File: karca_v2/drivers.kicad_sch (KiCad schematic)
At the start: 15 parts, among them J10 Keyhole ignition switch, J8 Screw_Terminal_01x10, J9 Screw_Terminal_01x04, Q7 IRF3708

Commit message: updated
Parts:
- removed D24: D_Schottky, Diode_SMD:D_SMA, symbol Device:D_Schottky

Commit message: Version alpha
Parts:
- removed BZ1: Buzzer, symbol Device:Buzzer
- removed Q7: IRF3708, symbol Simulation_SPICE:NMOS
- added F7: Fuse, Fuse:Fuse_1812_4532Metric, symbol Device:Fuse
- added J12: Buzzer, terminal blocks:P-2604-1102, symbol Connector:Screw_Terminal_01x02
- added Q4: IRF3708, IRF3708:TO254P1041X444X1930-3, symbol Simulation_SPICE:NMOS
- J10: footprint (none) -> terminal blocks:P-2604-1102
- J11: renamed from J9; footprint (none) -> terminal blocks:P-2604-1104
- J9: renamed from J8; footprint (none) -> terminal blocks:P-2604-1110
- R12: renamed from R3; value 910 -> 1k; footprint (none) -> Resistor_SMD:R_1206_3216Metric
- R13: renamed from R34; value 910 -> 1k; footprint (none) -> Resistor_SMD:R_1206_3216Metric
- R14: renamed from R44; footprint (none) -> Resistor_SMD:R_1206_3216Metric
- R15: renamed from R45; footprint (none) -> Resistor_SMD:R_1206_3216Metric
- R16: renamed from R39; footprint (none) -> Resistor_SMD:R_1206_3216Metric
- R17: renamed from R40; footprint (none) -> Resistor_SMD:R_1206_3216Metric
- TP22: renamed from TP42; footprint (none) -> TestPoint:TestPoint_Pad_D2.0mm
- renumbered D5 to D7, D23 to D8
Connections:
- net +12V: now also F7.1; no longer D7.2 (A), D8.2 (A), J10.1 (Pin_1)
- net GND: now also J12.2 (Pin_2), Q4.3 (S)
- net IGN_POS: now reaches J10.2 (Pin_2), J11.2 (Pin_2)
- net IGN_POS: now also D7.2 (A), D8.2 (A), J10.1 (Pin_1), F7.2, J12.1 (Pin_1)
- net IGN_NEG: now reaches J11.3 (Pin_3), R14.1
- net IGN_NEG: now also R13.2, Q4.2 (D)
- net at R16.2, TP22.1: now also Q4.1 (G)
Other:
- sheet current monitor ports: added DRV1_ADC, DRV2_ADC, DRV3_ADC, DRV4_ADC, DRV5_ADC, DRV5_TVS; removed CS, DRV_CLK, DRV_MISO, DRV_MOSI
- moved on the sheet: D7, D8, R12, R13, R14, R15, R16, R17, TP22

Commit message: discrete traces
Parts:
- renumbered F7 to F2, Q4 to Q3
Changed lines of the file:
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@@
   (symbol (lib_id "power:+12V") (at 214.63 135.89 0) (unit 1)
     (in_bom yes) (on_board yes) (dnp no) (fields_autoplaced)
-    (property "Reference" "#PWR052" (at 214.63 139.7 0)
+    (property "Reference" "#PWR063" (at 214.63 139.7 0)
       (effects (font (size 1.27 1.27)) hide)
     )
@@
       (project "karca_v2"
         (path "/29cf4797-56f2-4f57-ae95-7df639362e3c/7dac9c60-d103-4efb-8cad-8e42b4335148"
-          (reference "#PWR052") (unit 1)
+          (reference "#PWR063") (unit 1)
         )
       )
@@
   (symbol (lib_id "power:GND") (at 78.74 180.34 0) (unit 1)
     (in_bom yes) (on_board yes) (dnp no) (fields_autoplaced)
-    (property "Reference" "#PWR057" (at 78.74 186.69 0)
+    (property "Reference" "#PWR068" (at 78.74 186.69 0)
       (effects (font (size 1.27 1.27)) hide)
     )
@@
       (project "karca_v2"
         (path "/29cf4797-56f2-4f57-ae95-7df639362e3c/7dac9c60-d103-4efb-8cad-8e42b4335148"
-          (reference "#PWR057") (unit 1)
+          (reference "#PWR068") (unit 1)
         )
       )
@@
   (symbol (lib_id "power:GND") (at 140.335 174.625 0) (unit 1)
     (in_bom yes) (on_board yes) (dnp no) (fields_autoplaced)
-    (property "Reference" "#PWR056" (at 140.335 180.975 0)
+    (property "Reference" "#PWR067" (at 140.335 180.975 0)
       (effects (font (size 1.27 1.27)) hide)
     )
@@
       (project "karca_v2"
         (path "/29cf4797-56f2-4f57-ae95-7df639362e3c/7dac9c60-d103-4efb-8cad-8e42b4335148"
-          (reference "#PWR056") (unit 1)
+          (reference "#PWR067") (unit 1)
         )
       )
@@
   (symbol (lib_id "power:GND") (at 68.58 153.67 0) (unit 1)
     (in_bom yes) (on_board yes) (dnp no) (fields_autoplaced)
-    (property "Reference" "#PWR053" (at 68.58 160.02 0)
+    (property "Reference" "#PWR065" (at 68.58 160.02 0)
       (effects (font (size 1.27 1.27)) hide)
     )
@@
       (project "karca_v2"
         (path "/29cf4797-56f2-4f57-ae95-7df639362e3c/7dac9c60-d103-4efb-8cad-8e42b4335148"
-          (reference "#PWR053") (unit 1)
+          (reference "#PWR065") (unit 1)
         )
       )
@@
   (symbol (lib_id "power:+12V") (at 78.74 128.27 0) (unit 1)
     (in_bom yes) (on_board yes) (dnp no)
-    (property "Reference" "#PWR051" (at 78.74 132.08 0)
+    (property "Reference" "#PWR062" (at 78.74 132.08 0)
       (effects (font (size 1.27 1.27)) hide)
     )
@@
       (project "karca_v2"
         (path "/29cf4797-56f2-4f57-ae95-7df639362e3c/7dac9c60-d103-4efb-8cad-8e42b4335148"
-          (reference "#PWR051") (unit 1)
+          (reference "#PWR062") (unit 1)
         )
       )
@@
   (symbol (lib_id "power:GND") (at 118.11 161.29 0) (unit 1)
     (in_bom yes) (on_board yes) (dnp no) (fields_autoplaced)
-    (property "Reference" "#PWR055" (at 118.11 167.64 0)
+    (property "Reference" "#PWR066" (at 118.11 167.64 0)
       (effects (font (size 1.27 1.27)) hide)
     )
@@
       (project "karca_v2"
         (path "/29cf4797-56f2-4f57-ae95-7df639362e3c/7dac9c60-d103-4efb-8cad-8e42b4335148"
-          (reference "#PWR055") (unit 1)
+          (reference "#PWR066") (unit 1)
         )
       )
@@
   (symbol (lib_id "Device:Fuse") (at 78.74 132.08 0) (unit 1)
     (in_bom yes) (on_board yes) (dnp no) (fields_autoplaced)
-    (property "Reference" "F7" (at 81.28 130.81 0)
+    (property "Reference" "F2" (at 81.28 130.81 0)
       (effects (font (size 1.27 1.27)) (justify left))
     )
@@
       (project "karca_v2"
         (path "/29cf4797-56f2-4f57-ae95-7df639362e3c/7dac9c60-d103-4efb-8cad-8e42b4335148"
-          (reference "F7") (unit 1)
+          (reference "F2") (unit 1)
         )
       )
@@
   (symbol (lib_id "power:GND") (at 214.63 149.86 0) (unit 1)
     (in_bom yes) (on_board yes) (dnp no) (fields_autoplaced)
-    (property "Reference" "#PWR054" (at 214.63 156.21 0)
+    (property "Reference" "#PWR064" (at 214.63 156.21 0)
       (effects (font (size 1.27 1.27)) hide)
     )
@@
       (project "karca_v2"
         (path "/29cf4797-56f2-4f57-ae95-7df639362e3c/7dac9c60-d103-4efb-8cad-8e42b4335148"
-          (reference "#PWR054") (unit 1)
+          (reference "#PWR064") (unit 1)
         )
       )
@@
   (symbol (lib_id "Simulation_SPICE:NMOS") (at 76.2 171.45 0) (unit 1)
     (in_bom yes) (on_board yes) (dnp no) (fields_autoplaced)
-    (property "Reference" "Q4" (at 81.915 170.18 0)
+    (property "Reference" "Q3" (at 81.915 170.18 0)
       (effects (font (size 1.27 1.27)) (justify left))
     )
@@
       (project "karca_v2"
         (path "/29cf4797-56f2-4f57-ae95-7df639362e3c/7dac9c60-d103-4efb-8cad-8e42b4335148"
-          (reference "Q4") (unit 1)
-        )
-      )
+          (reference "Q3") (unit 1)
+        )
+      )

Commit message: fixed violations
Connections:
- net IGN_POS: no longer J10.2 (Pin_2), J11.2 (Pin_2), J12.1 (Pin_1)
- new net IGN_POS_OUT: J10.2 (Pin_2), J11.2 (Pin_2), J12.1 (Pin_1)
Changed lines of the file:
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@@
   (junction (at 78.74 180.34) (diameter 0) (color 0 0 0 0)
   )
+  (junction (at 170.815 130.81) (diameter 0) (color 0 0 0 0)
+  )
   (junction (at 64.135 171.45) (diameter 0) (color 0 0 0 0)
   )
@@
   (junction (at 140.335 153.67) (diameter 0) (color 0 0 0 0)
   )
-  (junction (at 115.57 135.89) (diameter 0) (color 0 0 0 0)
+  (wire (pts (xy 170.815 130.81) (xy 170.815 151.13))
+    (stroke (width 0) (type default))
   )
   (wire (pts (xy 140.335 173.355) (xy 140.335 174.625))
@@
     (stroke (width 0) (type default))
   )
-  (wire (pts (xy 115.57 135.89) (xy 165.1 135.89))
-    (stroke (width 0) (type default))
-  )
   (wire (pts (xy 214.63 147.32) (xy 214.63 149.86))
     (stroke (width 0) (type default))
@@
     (stroke (width 0) (type default))
   )
-  (wire (pts (xy 115.57 156.21) (xy 118.11 156.21))
+  (wire (pts (xy 170.815 151.13) (xy 173.355 151.13))
     (stroke (width 0) (type default))
   )
@@
     (stroke (width 0) (type default))
   )
-  (wire (pts (xy 78.74 135.89) (xy 115.57 135.89))
+  (wire (pts (xy 78.74 135.89) (xy 165.1 135.89))
     (stroke (width 0) (type default))
   )
@@
     (stroke (width 0) (type default))
   )
+  (wire (pts (xy 170.815 130.81) (xy 173.355 130.81))
+    (stroke (width 0) (type default))
+  )
   (wire (pts (xy 232.41 60.96) (xy 231.14 60.96))
     (stroke (width 0) (type default))
@@
     (stroke (width 0) (type default))
   )
-  (wire (pts (xy 115.57 135.89) (xy 115.57 156.21))
+  (wire (pts (xy 173.355 153.67) (xy 173.355 156.21))
     (stroke (width 0) (type default))
   )
@@
     (stroke (width 0) (type default))
   )
-  (wire (pts (xy 167.64 130.81) (xy 173.355 130.81))
+  (wire (pts (xy 167.64 130.81) (xy 170.815 130.81))
     (stroke (width 0) (type default))
   )
   (wire (pts (xy 232.41 68.58) (xy 226.06 68.58))
-    (stroke (width 0) (type default))
-  )
-  (wire (pts (xy 118.11 158.75) (xy 118.11 161.29))
     (stroke (width 0) (type default))
   )
@@
     (effects (font (size 1.27 1.27)) (justify right bottom))
   )
-  (label "IGN_POS" (at 212.725 142.24 90) (fields_autoplaced)
+  (label "IGN_POS_OUT" (at 212.725 142.24 90) (fields_autoplaced)
     (effects (font (size 1.27 1.27)) (justify left bottom))
   )
@@
         (path "/29cf4797-56f2-4f57-ae95-7df639362e3c/7dac9c60-d103-4efb-8cad-8e42b4335148"
           (reference "#PWR076") (unit 1)
+        )
+      )
+    )
+  )
+  (symbol (lib_id "Connector:Screw_Terminal_01x02") (at 178.435 151.13 0) (unit 1)
+    (in_bom yes) (on_board yes) (dnp no)
+    (property "Reference" "J12" (at 180.975 151.13 0)
+      (effects (font (size 1.27 1.27)) (justify left))
+    )
+    (property "Value" "Buzzer" (at 175.895 156.21 0)
+      (effects (font (size 1.27 1.27)) (justify left))
+    )
+    (property "Footprint" "terminal blocks:P-2604-1102" (at 178.435 151.13 0)
+      (effects (font (size 1.27 1.27)) hide)
+    )
+    (property "Datasheet" "~" (at 178.435 151.13 0)
+      (effects (font (size 1.27 1.27)) hide)
+    )
+    (pin "2")
+    (pin "1")
+    (instances
+      (project "karca_v2"
+        (path "/29cf4797-56f2-4f57-ae95-7df639362e3c/7dac9c60-d103-4efb-8cad-8e42b4335148"
+          (reference "J12") (unit 1)
         )
       )
@@
         (path "/29cf4797-56f2-4f57-ae95-7df639362e3c/7dac9c60-d103-4efb-8cad-8e42b4335148"
           (reference "D7") (unit 1)
-        )
-      )
-    )
-  )
-  (symbol (lib_id "power:GND") (at 118.11 161.29 0) (unit 1)
-    (in_bom yes) (on_board yes) (dnp no) (fields_autoplaced)
-    (property "Reference" "#PWR074" (at 118.11 167.64 0)
-      (effects (font (size 1.27 1.27)) hide)
-    )
-    (property "Value" "GND" (at 118.11 166.37 0)
-      (effects (font (size 1.27 1.27)))
-    )
-    (property "Footprint" "" (at 118.11 161.29 0)
-      (effects (font (size 1.27 1.27)) hide)
-    )
-    (property "Datasheet" "" (at 118.11 161.29 0)
-      (effects (font (size 1.27 1.27)) hide)
-    )
-    (pin "1")
-    (instances
-      (project "karca_v2"
-        (path "/29cf4797-56f2-4f57-ae95-7df639362e3c/7dac9c60-d103-4efb-8cad-8e42b4335148"
-          (reference "#PWR074") (unit 1)
         )
       )
@@
     )
   )
-  (symbol (lib_id "Connector:Screw_Terminal_01x02") (at 123.19 156.21 0) (unit 1)
-    (in_bom yes) (on_board yes) (dnp no)
-    (property "Reference" "J12" (at 125.73 156.21 0)
-      (effects (font (size 1.27 1.27)) (justify left))
-    )
-    (property "Value" "Buzzer" (at 120.65 161.29 0)
-      (effects (font (size 1.27 1.27)) (justify left))
-    )
-    (property "Footprint" "terminal blocks:P-2604-1102" (at 123.19 156.21 0)
-      (effects (font (size 1.27 1.27)) hide)
-    )
-    (property "Datasheet" "~" (at 123.19 156.21 0)
-      (effects (font (size 1.27 1.27)) hide)
-    )
-    (pin "2")
-    (pin "1")
-    (instances
-      (project "karca_v2"
-        (path "/29cf4797-56f2-4f57-ae95-7df639362e3c/7dac9c60-d103-4efb-8cad-8e42b4335148"
-          (reference "J12") (unit 1)
-        )
-      )
-    )
-  )
   (symbol (lib_id "Connector:TestPoint") (at 64.135 171.45 0) (unit 1)
     (in_bom yes) (on_board yes) (dnp no)
@@
         )
       )
+    )
+  )
+  (symbol (lib_id "power:GND") (at 173.355 156.21 0) (unit 1)
+    (in_bom yes) (on_board yes) (dnp no) (fields_autoplaced)
+    (property "Reference" "#PWR074" (at 173.355 162.56 0)
+      (effects (font (size 1.27 1.27)) hide)
+    )
+    (property "Value" "GND" (at 173.355 161.29 0)
+      (effects (font (size 1.27 1.27)))
+    )
+    (property "Footprint" "" (at 173.355 156.21 0)
+      (effects (font (size 1.27 1.27)) hide)
+    )
+    (property "Datasheet" "" (at 173.355 156.21 0)
+      (effects (font (size 1.27 1.27)) hide)
+    )
+    (pin "1")
+    (instances
+      (project "karca_v2"
+        (path "/29cf4797-56f2-4f57-ae95-7df639362e3c/7dac9c60-d103-4efb-8cad-8e42b4335148"
+          (reference "#PWR074") (unit 1)
+        )
+      )

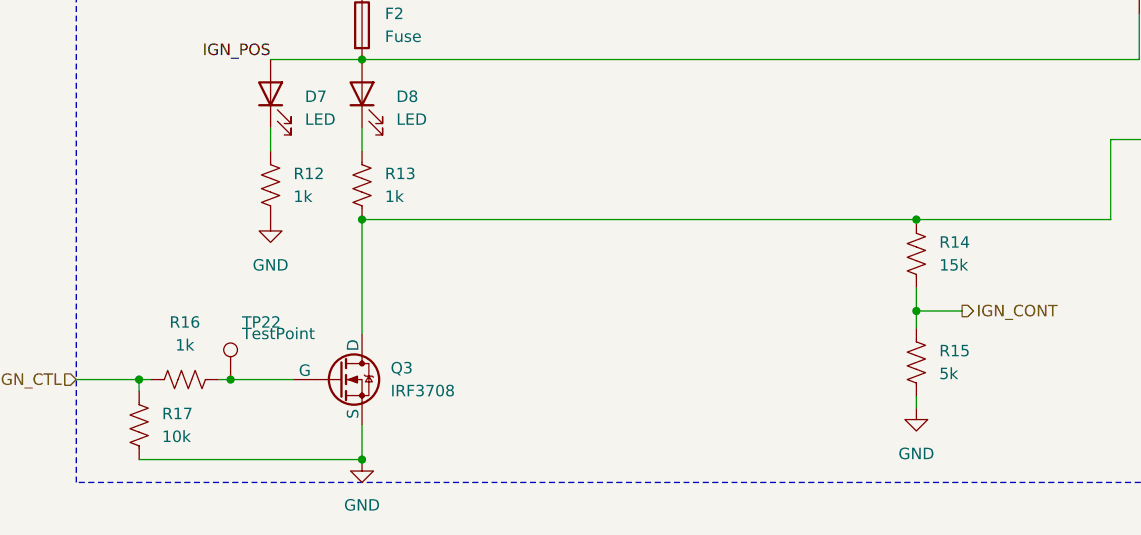
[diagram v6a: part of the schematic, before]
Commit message: Fixed ground capacitors
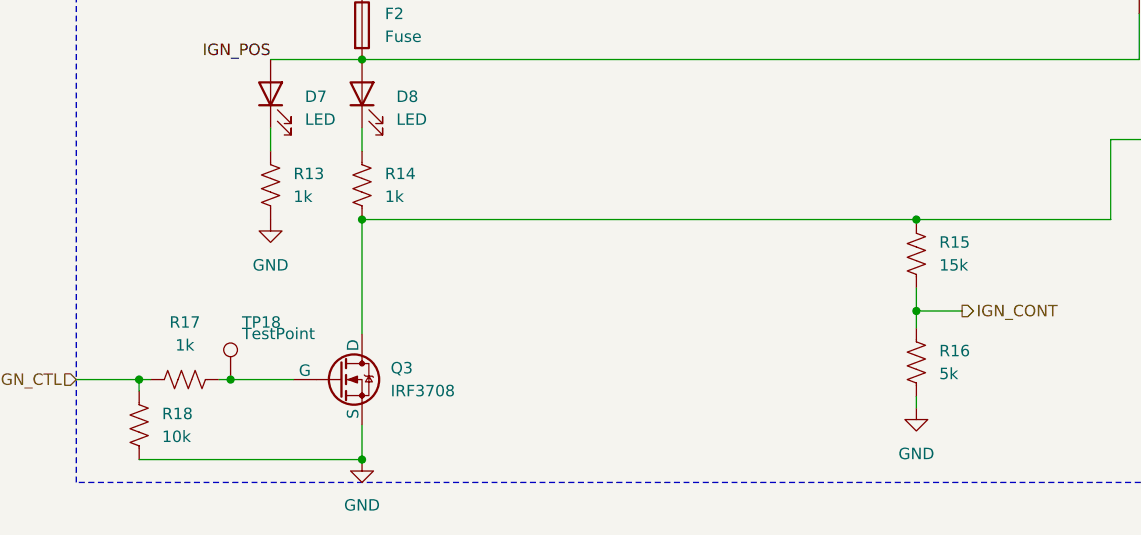
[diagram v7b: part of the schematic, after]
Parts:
- renumbered R12 to R13, R13 to R14, R14 to R15, R15 to R16, R16 to R17, R17 to R18, TP22 to TP18
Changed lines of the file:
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@@
   (symbol (lib_id "power:+12V") (at 214.63 135.89 0) (unit 1)
     (in_bom yes) (on_board yes) (dnp no) (fields_autoplaced)
-    (property "Reference" "#PWR071" (at 214.63 139.7 0)
+    (property "Reference" "#PWR067" (at 214.63 139.7 0)
       (effects (font (size 1.27 1.27)) hide)
     )
@@
       (project "karca_v2"
         (path "/29cf4797-56f2-4f57-ae95-7df639362e3c/7dac9c60-d103-4efb-8cad-8e42b4335148"
-          (reference "#PWR071") (unit 1)
+          (reference "#PWR067") (unit 1)
         )
       )
@@
   (symbol (lib_id "power:GND") (at 78.74 180.34 0) (unit 1)
     (in_bom yes) (on_board yes) (dnp no) (fields_autoplaced)
-    (property "Reference" "#PWR076" (at 78.74 186.69 0)
+    (property "Reference" "#PWR072" (at 78.74 186.69 0)
       (effects (font (size 1.27 1.27)) hide)
     )
@@
       (project "karca_v2"
         (path "/29cf4797-56f2-4f57-ae95-7df639362e3c/7dac9c60-d103-4efb-8cad-8e42b4335148"
-          (reference "#PWR076") (unit 1)
+          (reference "#PWR072") (unit 1)
         )
       )
@@
   (symbol (lib_id "power:GND") (at 140.335 174.625 0) (unit 1)
     (in_bom yes) (on_board yes) (dnp no) (fields_autoplaced)
-    (property "Reference" "#PWR075" (at 140.335 180.975 0)
+    (property "Reference" "#PWR071" (at 140.335 180.975 0)
       (effects (font (size 1.27 1.27)) hide)
     )
@@
       (project "karca_v2"
         (path "/29cf4797-56f2-4f57-ae95-7df639362e3c/7dac9c60-d103-4efb-8cad-8e42b4335148"
-          (reference "#PWR075") (unit 1)
+          (reference "#PWR071") (unit 1)
         )
       )
@@
   (symbol (lib_id "power:GND") (at 68.58 153.67 0) (unit 1)
     (in_bom yes) (on_board yes) (dnp no) (fields_autoplaced)
-    (property "Reference" "#PWR073" (at 68.58 160.02 0)
+    (property "Reference" "#PWR069" (at 68.58 160.02 0)
       (effects (font (size 1.27 1.27)) hide)
     )
@@
       (project "karca_v2"
         (path "/29cf4797-56f2-4f57-ae95-7df639362e3c/7dac9c60-d103-4efb-8cad-8e42b4335148"
-          (reference "#PWR073") (unit 1)
+          (reference "#PWR069") (unit 1)
         )
       )
@@
   (symbol (lib_id "power:+12V") (at 78.74 128.27 0) (unit 1)
     (in_bom yes) (on_board yes) (dnp no)
-    (property "Reference" "#PWR070" (at 78.74 132.08 0)
+    (property "Reference" "#PWR066" (at 78.74 132.08 0)
       (effects (font (size 1.27 1.27)) hide)
     )
@@
       (project "karca_v2"
         (path "/29cf4797-56f2-4f57-ae95-7df639362e3c/7dac9c60-d103-4efb-8cad-8e42b4335148"
-          (reference "#PWR070") (unit 1)
+          (reference "#PWR066") (unit 1)
         )
       )
@@
   (symbol (lib_id "Device:R_US") (at 68.58 149.86 0) (unit 1)
     (in_bom yes) (on_board yes) (dnp no) (fields_autoplaced)
-    (property "Reference" "R12" (at 71.12 148.59 0)
+    (property "Reference" "R13" (at 71.12 148.59 0)
       (effects (font (size 1.27 1.27)) (justify left))
     )
@@
       (project "karca_v2"
         (path "/29cf4797-56f2-4f57-ae95-7df639362e3c/7dac9c60-d103-4efb-8cad-8e42b4335148"
-          (reference "R12") (unit 1)
+          (reference "R13") (unit 1)
         )
       )
@@
   (symbol (lib_id "Device:R_US") (at 140.335 157.48 0) (unit 1)
     (in_bom yes) (on_board yes) (dnp no) (fields_autoplaced)
-    (property "Reference" "R14" (at 142.875 156.21 0)
+    (property "Reference" "R15" (at 142.875 156.21 0)
       (effects (font (size 1.27 1.27)) (justify left))
     )
@@
       (project "karca_v2"
         (path "/29cf4797-56f2-4f57-ae95-7df639362e3c/7dac9c60-d103-4efb-8cad-8e42b4335148"
-          (reference "R14") (unit 1)
+          (reference "R15") (unit 1)
         )
       )
@@
   (symbol (lib_id "power:GND") (at 214.63 149.86 0) (unit 1)
     (in_bom yes) (on_board yes) (dnp no) (fields_autoplaced)
-    (property "Reference" "#PWR072" (at 214.63 156.21 0)
+    (property "Reference" "#PWR068" (at 214.63 156.21 0)
       (effects (font (size 1.27 1.27)) hide)
     )
@@
       (project "karca_v2"
         (path "/29cf4797-56f2-4f57-ae95-7df639362e3c/7dac9c60-d103-4efb-8cad-8e42b4335148"
-          (reference "#PWR072") (unit 1)
+          (reference "#PWR068") (unit 1)
         )
       )
@@
   (symbol (lib_id "Connector:TestPoint") (at 64.135 171.45 0) (unit 1)
     (in_bom yes) (on_board yes) (dnp no)
-    (property "Reference" "TP22" (at 65.405 165.1 0)
+    (property "Reference" "TP18" (at 65.405 165.1 0)
       (effects (font (size 1.27 1.27)) (justify left))
     )
@@
       (project "karca_v2"
         (path "/29cf4797-56f2-4f57-ae95-7df639362e3c/7dac9c60-d103-4efb-8cad-8e42b4335148"
-          (reference "TP22") (unit 1)
+          (reference "TP18") (unit 1)
         )
       )
@@
   (symbol (lib_id "Device:R_US") (at 140.335 169.545 0) (unit 1)
     (in_bom yes) (on_board yes) (dnp no) (fields_autoplaced)
-    (property "Reference" "R15" (at 142.875 168.275 0)
+    (property "Reference" "R16" (at 142.875 168.275 0)
       (effects (font (size 1.27 1.27)) (justify left))
     )
@@
       (project "karca_v2"
         (path "/29cf4797-56f2-4f57-ae95-7df639362e3c/7dac9c60-d103-4efb-8cad-8e42b4335148"
-          (reference "R15") (unit 1)
+          (reference "R16") (unit 1)
         )
       )
@@
   (symbol (lib_id "Device:R_US") (at 78.74 149.86 0) (unit 1)
     (in_bom yes) (on_board yes) (dnp no) (fields_autoplaced)
-    (property "Reference" "R13" (at 81.28 148.59 0)
+    (property "Reference" "R14" (at 81.28 148.59 0)
       (effects (font (size 1.27 1.27)) (justify left))
     )
@@
       (project "karca_v2"
         (path "/29cf4797-56f2-4f57-ae95-7df639362e3c/7dac9c60-d103-4efb-8cad-8e42b4335148"
-          (reference "R13") (unit 1)
+          (reference "R14") (unit 1)
         )
       )
@@
   (symbol (lib_id "power:GND") (at 173.355 156.21 0) (unit 1)
     (in_bom yes) (on_board yes) (dnp no) (fields_autoplaced)
-    (property "Reference" "#PWR074" (at 173.355 162.56 0)
+    (property "Reference" "#PWR070" (at 173.355 162.56 0)
       (effects (font (size 1.27 1.27)) hide)
     )
@@
       (project "karca_v2"
         (path "/29cf4797-56f2-4f57-ae95-7df639362e3c/7dac9c60-d103-4efb-8cad-8e42b4335148"
-          (reference "#PWR074") (unit 1)
+          (reference "#PWR070") (unit 1)
         )
       )
@@
   (symbol (lib_id "Device:R_US") (at 59.055 171.45 90) (unit 1)
     (in_bom yes) (on_board yes) (dnp no) (fields_autoplaced)
-    (property "Reference" "R16" (at 59.055 165.1 90)
+    (property "Reference" "R17" (at 59.055 165.1 90)
       (effects (font (size 1.27 1.27)))
     )
@@
       (project "karca_v2"
         (path "/29cf4797-56f2-4f57-ae95-7df639362e3c/7dac9c60-d103-4efb-8cad-8e42b4335148"
-          (reference "R16") (unit 1)
+          (reference "R17") (unit 1)
         )
       )
@@
   (symbol (lib_id "Device:R_US") (at 53.975 176.53 0) (unit 1)
     (in_bom yes) (on_board yes) (dnp no) (fields_autoplaced)
-    (property "Reference" "R17" (at 56.515 175.26 0)
+    (property "Reference" "R18" (at 56.515 175.26 0)
       (effects (font (size 1.27 1.27)) (justify left))
     )
@@
       (project "karca_v2"
         (path "/29cf4797-56f2-4f57-ae95-7df639362e3c/7dac9c60-d103-4efb-8cad-8e42b4335148"
-          (reference "R17") (unit 1)
-        )
-      )
+          (reference "R18") (unit 1)
+        )
+      )
